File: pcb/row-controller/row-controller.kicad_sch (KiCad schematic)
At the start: 35 parts, among them IC1 INA220BIDGSR, IC2 THVD1420DR, IC3 THVD1420DR, J1 Power In, J3 Power Row, J5 Row Bus Header, J6 Tile Bus Header, U1 XAIO RP2350, U2 R-78E5.0-0.5

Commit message: Fixed trace length for sense resistor.
Ensure the traces to IN+ and IN- go directly to those pins.  Electrically IN+ and Vbus connect, and since they are adjacent, I mistakenly wired the sense resistor to Vbus, with a dog leg over to IN+.  Flip that so it goes directly to IN+ with a dog leg to Vbus.  This keeps the line lengths for IN+ and IN- short and equal.
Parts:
- IC1: value INA220BIDGSR -> INA226; footprint INA220BIDGSR:SOP50P490X110-10N -> Package_SO:TSSOP-10_3x3mm_P0.5mm; symbol INA220BIDGSR:INA220BIDGSR -> Sensor_Energy:INA226
- R2, R3, R4, R5, R6, R7: symbol Device:R -> Device:R_US
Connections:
- net +3V3: now also C3.1; no longer C3.2
- net GND: now also C3.2; no longer C3.1
- no-connect marks 0 -> 1
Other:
- moved on the sheet: C8, C9, R1, U1

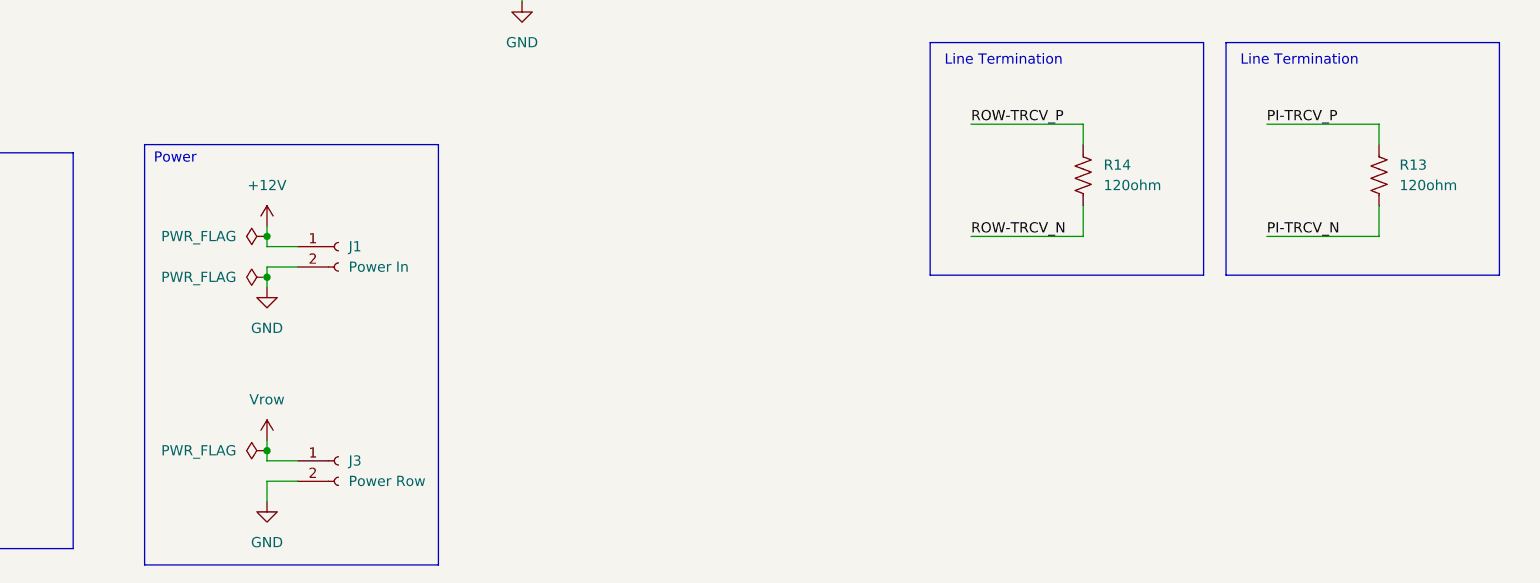
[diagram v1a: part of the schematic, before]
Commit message: Committing all PCB changes.  Everything has been sent and received from fab
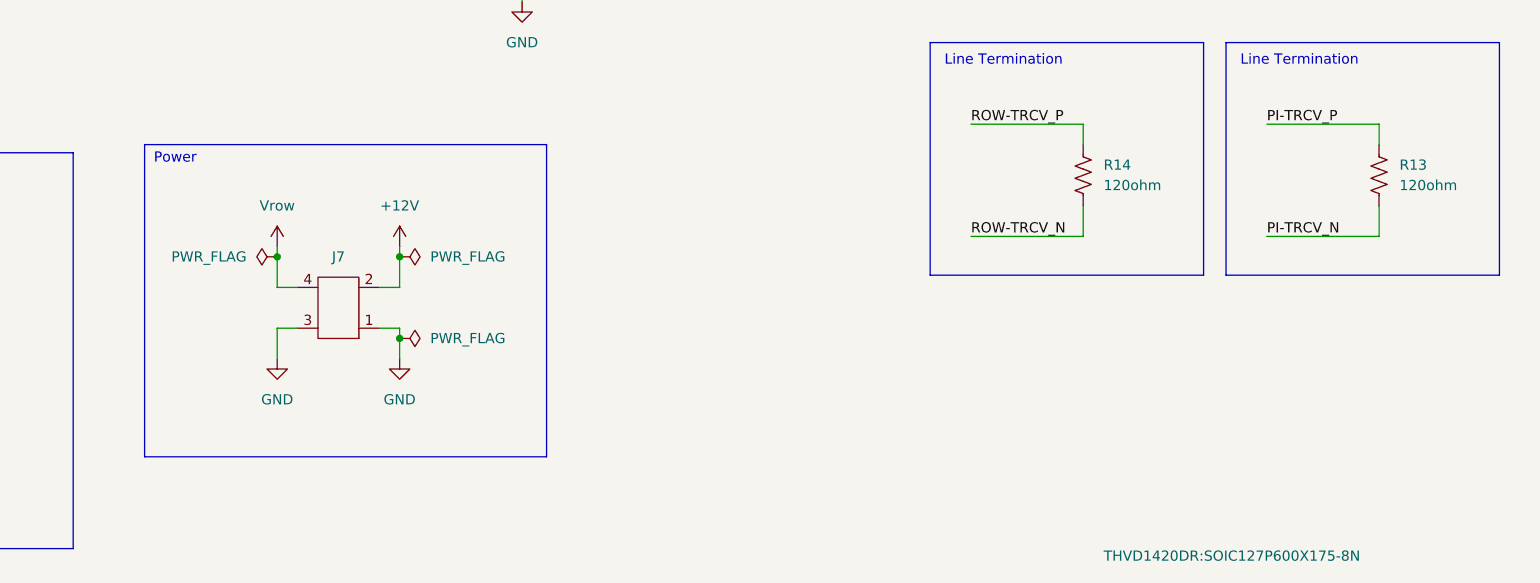
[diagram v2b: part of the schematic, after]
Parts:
- removed J1: Power In, Connector_JST:JST_XH_S2B-XH-A_1x02_P2.50mm_Horizontal, symbol Connector:Conn_01x02_Socket
- removed J3: Power Row, Connector_JST:JST_XH_S2B-XH-A_1x02_P2.50mm_Horizontal, symbol Connector:Conn_01x02_Socket
- added J7: (no value), Garth:Quad Powerpole, symbol Garth Libraries:Quad_Powerpole
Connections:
- net +12V: now also J7.2
- net GND: now also J7.1, J7.3
- net Vrow: now also J7.4
